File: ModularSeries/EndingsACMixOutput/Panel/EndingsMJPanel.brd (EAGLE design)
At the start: 48.5 x 100 mm, 12 parts

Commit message: Fields added and various updates to designs
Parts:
- removed 1V/OCT, FMCV, SINE, SQR, TRI: COMBI-JACKCINCHNANA, ElectricNoodleBox:NEWCOMBOJACK_PANEL
- removed BOARD1: PRISM_LINK, ElectricNoodleBox:PRISM
- removed R1, R2, R3, R4: B100K, ElectricNoodleBox:ALPHA_RV09_9MMPOT
- removed U$1, U$2: (no value), ElectricNoodleBox:LOGO20X20
- added E$10, E$11, E$2, E$7, E$8, E$9: (no value), ElectricNoodleBox:ALPHA9MM_POT_CUTOUT
- added E$12: (no value), ElectricNoodleBox:MINIJACK_M6_CUTOUT
- added E$13: (no value), ElectricNoodleBox:NEUTRIK_6.35_CUTOUT
- added E$14: (no value), ElectricNoodleBox:LOGO20X20
- added E$6: (no value), ElectricNoodleBox:CINCH_BANANA_CUTOUT
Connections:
- removed net AGND: 1V/OCT.S, BOARD1.GNDA, BOARD1.GNDB, FMCV.S, R1.LUGL, R1.LUGR, R2.LUGL, R2.LUGR, R3.C1, R3.LUGL, R3.LUGR, R4.LUGL, R4.LUGR, SINE.S, SQR.S, TRI.S
- removed net N$1: 1V/OCT.CONN, 1V/OCT.T1, 1V/OCT.T2, BOARD1.CVA
- removed net N$10: BOARD1.SIN, SINE.CONN, SINE.T1, SINE.T2
- removed net N$11: BOARD1.TRI, TRI.CONN, TRI.T1, TRI.T2
- removed net N$12: BOARD1.SQR, SQR.CONN, SQR.T1, SQR.T2
- removed net N$2: BOARD1.F1, R1.C1, R2.C1
- removed net N$3: BOARD1.F3, R1.C3, R2.C3
- removed net N$4: BOARD1.F2, R1.C2
- removed net N$5: BOARD1.FINE, R2.C2
- removed net N$6: FMCV.CONN, FMCV.T1, FMCV.T2, R3.C3
- removed net N$7: BOARD1.CVB, R3.C2
- removed net N$8: BOARD1.DIST1, R4.C1, R4.C2
- removed net N$9: BOARD1.DIST2, R4.C3
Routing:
- net AGND: track 202.4 -> 0.00 mm, vias 2 -> 0
- net S$2: track 0.00 -> 80.0 mm
- net S$1: track 0.00 -> 80.0 mm
- net N$6: track 71.8 -> 0.00 mm, vias 1 -> 0
- net N$8: track 67.2 -> 0.00 mm, vias 1 -> 0
- net N$9: track 65.8 -> 0.00 mm, vias 1 -> 0
- net N$1: track 65.1 -> 0.00 mm, vias 1 -> 0
- net N$11: track 63.3 -> 0.00 mm
- net N$5: track 62.7 -> 0.00 mm, vias 3 -> 0
- net N$2: track 62.4 -> 0.00 mm, vias 1 -> 0
- net N$3: track 60.6 -> 0.00 mm, vias 1 -> 0
- net N$12: track 57.4 -> 0.00 mm
- net N$7: track 38.7 -> 0.00 mm, vias 1 -> 0
- net N$10: track 34.8 -> 0.00 mm
- net N$4: track 29.1 -> 0.00 mm
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- added copper zone on layer 16, net GND
- removed copper zone on layer 1, net AGND
- removed copper zone on layer 16, net AGND
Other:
- board size 48.5 x 100 mm -> 50.5 x 128.5 mm
- board text added: "DEPARTURE"
- board text added: "E N D I N G S"
- board text added: "EARS"
- board text added: "F U S E"
- board text added: "MASS"
- board text added: "UNITE"
- board text removed: "Aidan Taylor 2020"
- board text removed: "Course"
- board text removed: "Distortion"
- board text removed: "FM Depth"
- board text removed: "Fine"
- board text removed: "Prism"
- board text removed: "Rev 1.2"
- board text removed: "Triangle Core Voltage Controlled Oscillator"

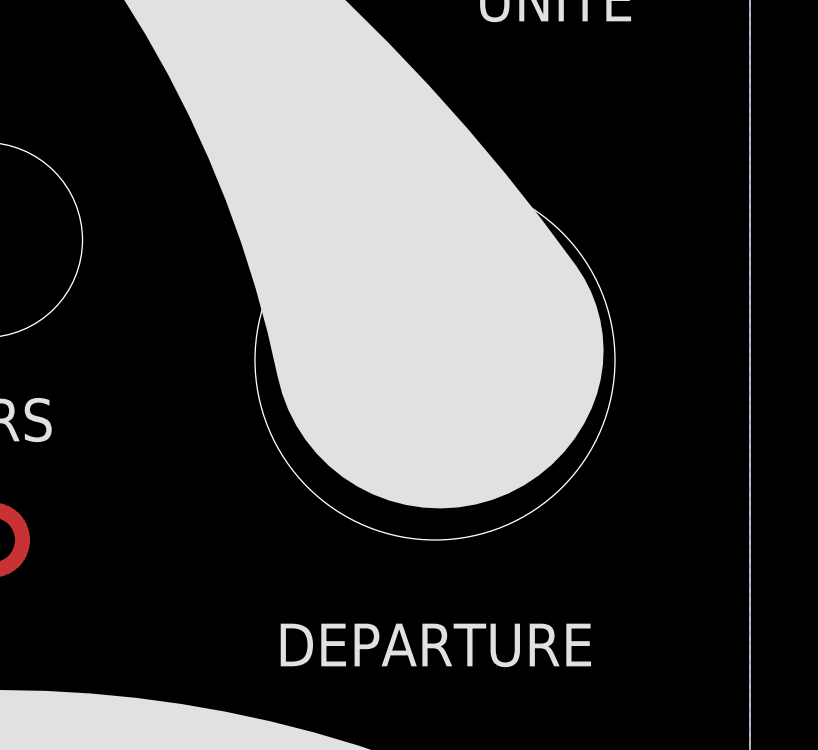
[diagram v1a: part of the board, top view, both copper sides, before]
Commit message: Fields module images and BOM added
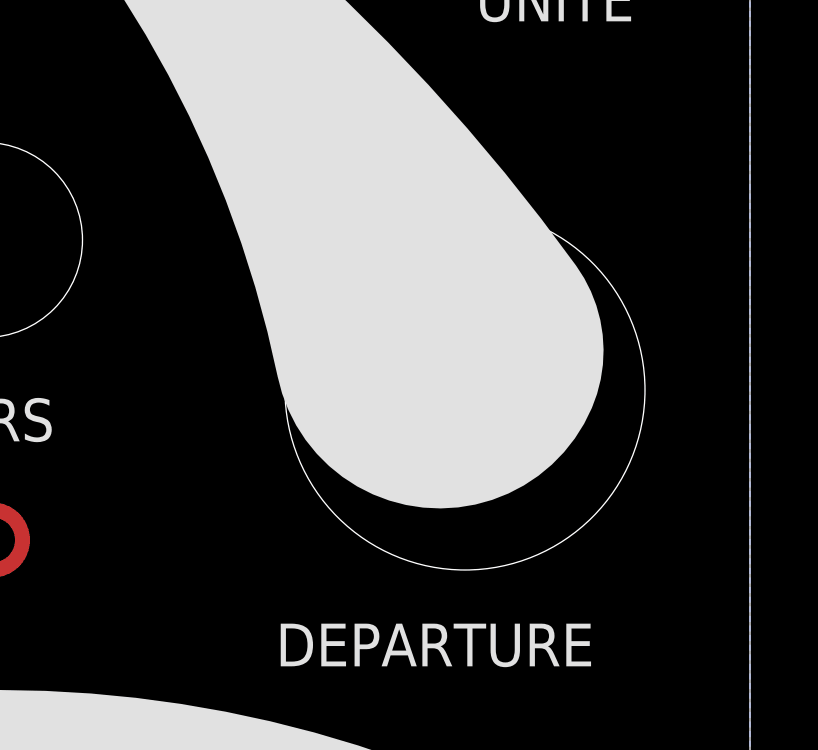
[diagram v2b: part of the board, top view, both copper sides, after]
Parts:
- moved E$13 1.41 mm to (41.0, 5.00)
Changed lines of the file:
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@@
 <element name="E$11" library="ElectricNoodleBox" package="ALPHA9MM_POT_CUTOUT" value="" x="9" y="10" smashed="yes"/>
 <element name="E$12" library="ElectricNoodleBox" package="MINIJACK_M6_CUTOUT" value="" x="25" y="10" smashed="yes"/>
-<element name="E$13" library="ElectricNoodleBox" package="NEUTRIK_6.35_CUTOUT" value="" x="40" y="6" smashed="yes"/>
+<element name="E$13" library="ElectricNoodleBox" package="NEUTRIK_6.35_CUTOUT" value="" x="41" y="5" smashed="yes"/>
 <element name="E$14" library="ElectricNoodleBox" package="LOGO20X20" value="" x="47" y="93.5" smashed="yes" rot="MR0"/>
 </elements>
